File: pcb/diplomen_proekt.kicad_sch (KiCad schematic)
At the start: 24 parts, among them SW1 SW_Push, U1 DA56-11SURKWA, U2 ESP32-S3, U3 HC-SR04, U4 ACTIVE_BUZZER, U5 TP4056, U6 MCP1826S

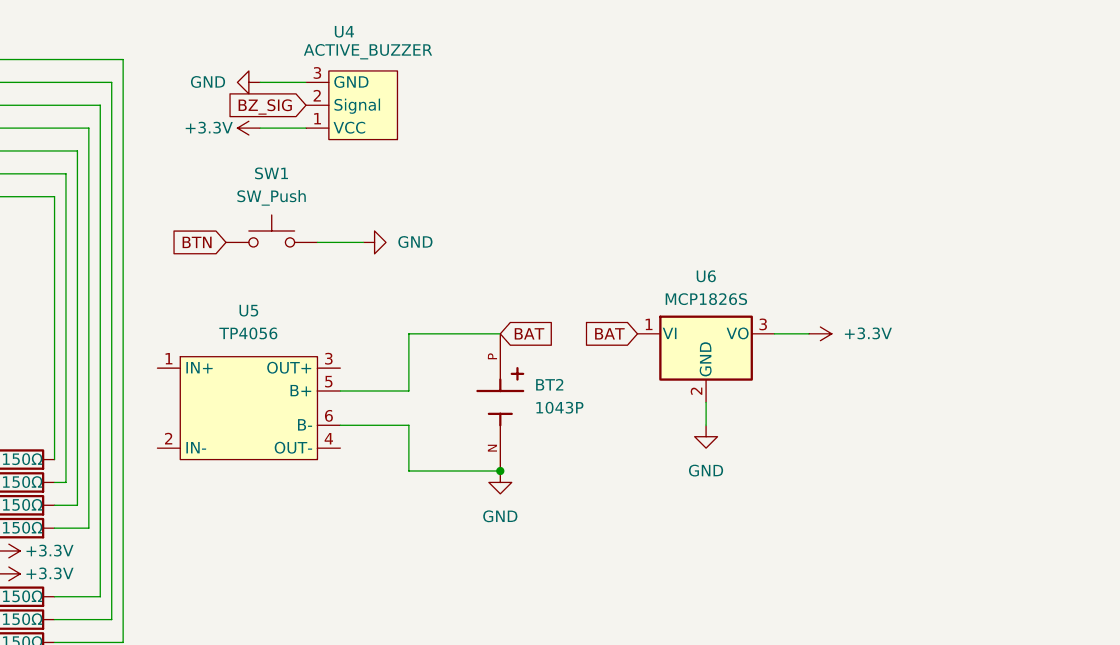
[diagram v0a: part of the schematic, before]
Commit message: Added capacitors
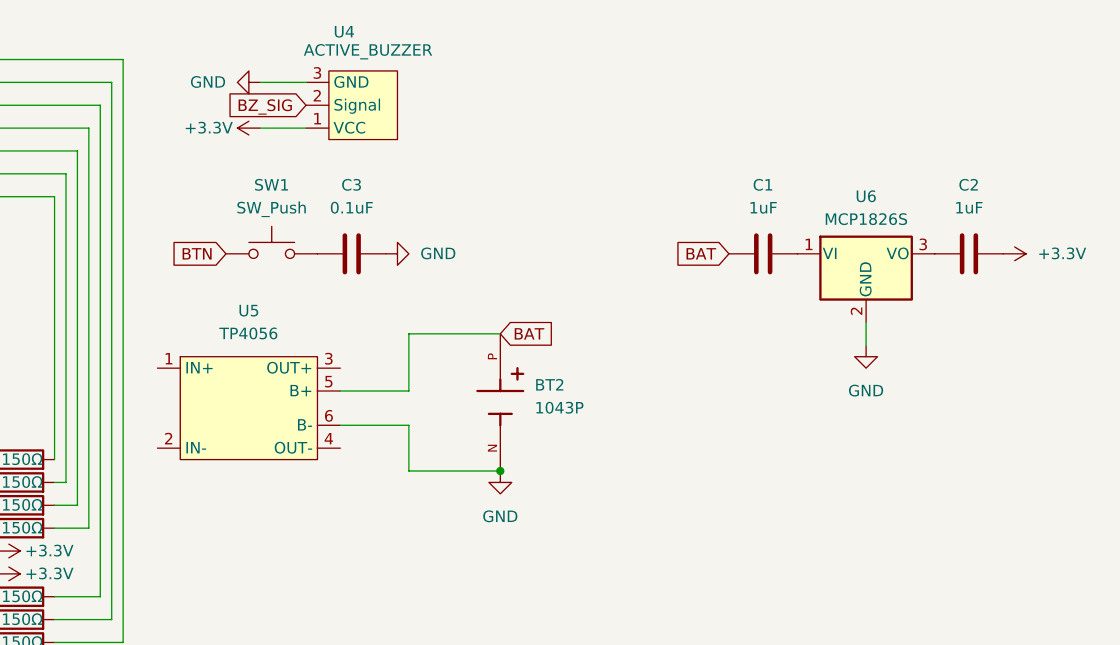
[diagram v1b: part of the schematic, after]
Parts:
- added C1, C2: 1uF, Capacitor_THT:CP_Radial_D5.0mm_P2.50mm, symbol Device:C
- added C3: 0.1uF, Capacitor_THT:CP_Radial_D5.0mm_P2.50mm, symbol Device:C
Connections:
- net +3.3V: now also C2.2; no longer U6.3 (VO)
- net BAT: now also C1.1; no longer U6.1 (VI)
- net GND: now also C3.2; no longer SW1.2
- new net: C1.2, U6.1 (VI)
- new net: C2.1, U6.3 (VO)
- new net: C3.1, SW1.2
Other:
- moved on the sheet: SW1, U6

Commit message: Added pcb images
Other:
- moved on the sheet: BT2, C1, C2, C3, SW1, U4, U5, U6
